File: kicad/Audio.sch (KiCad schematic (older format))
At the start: 14 parts, among them U4 OPA1664, U5 PGA4311, U6 OPA1664

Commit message: Adding untracked files
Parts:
- renumbered U4 to U3, U5 to U4, U6 to U5

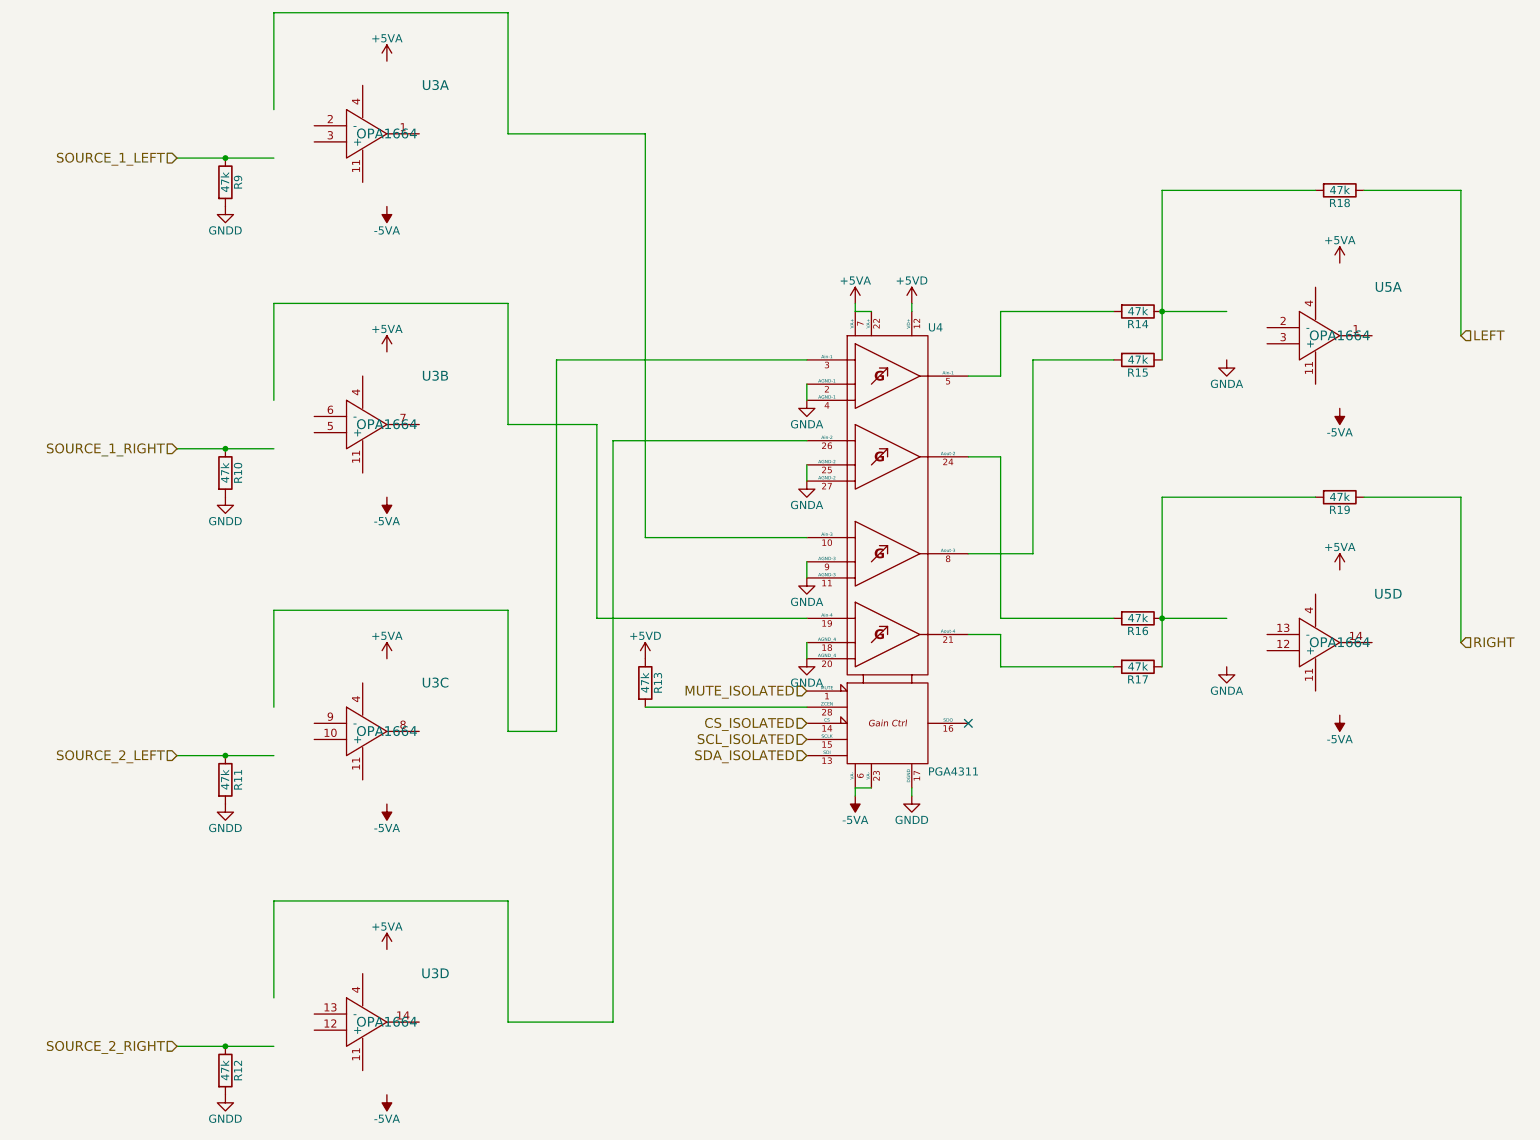
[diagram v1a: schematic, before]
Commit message: Reworked schematics to allow control of the power and introduction of ATMega328P for control
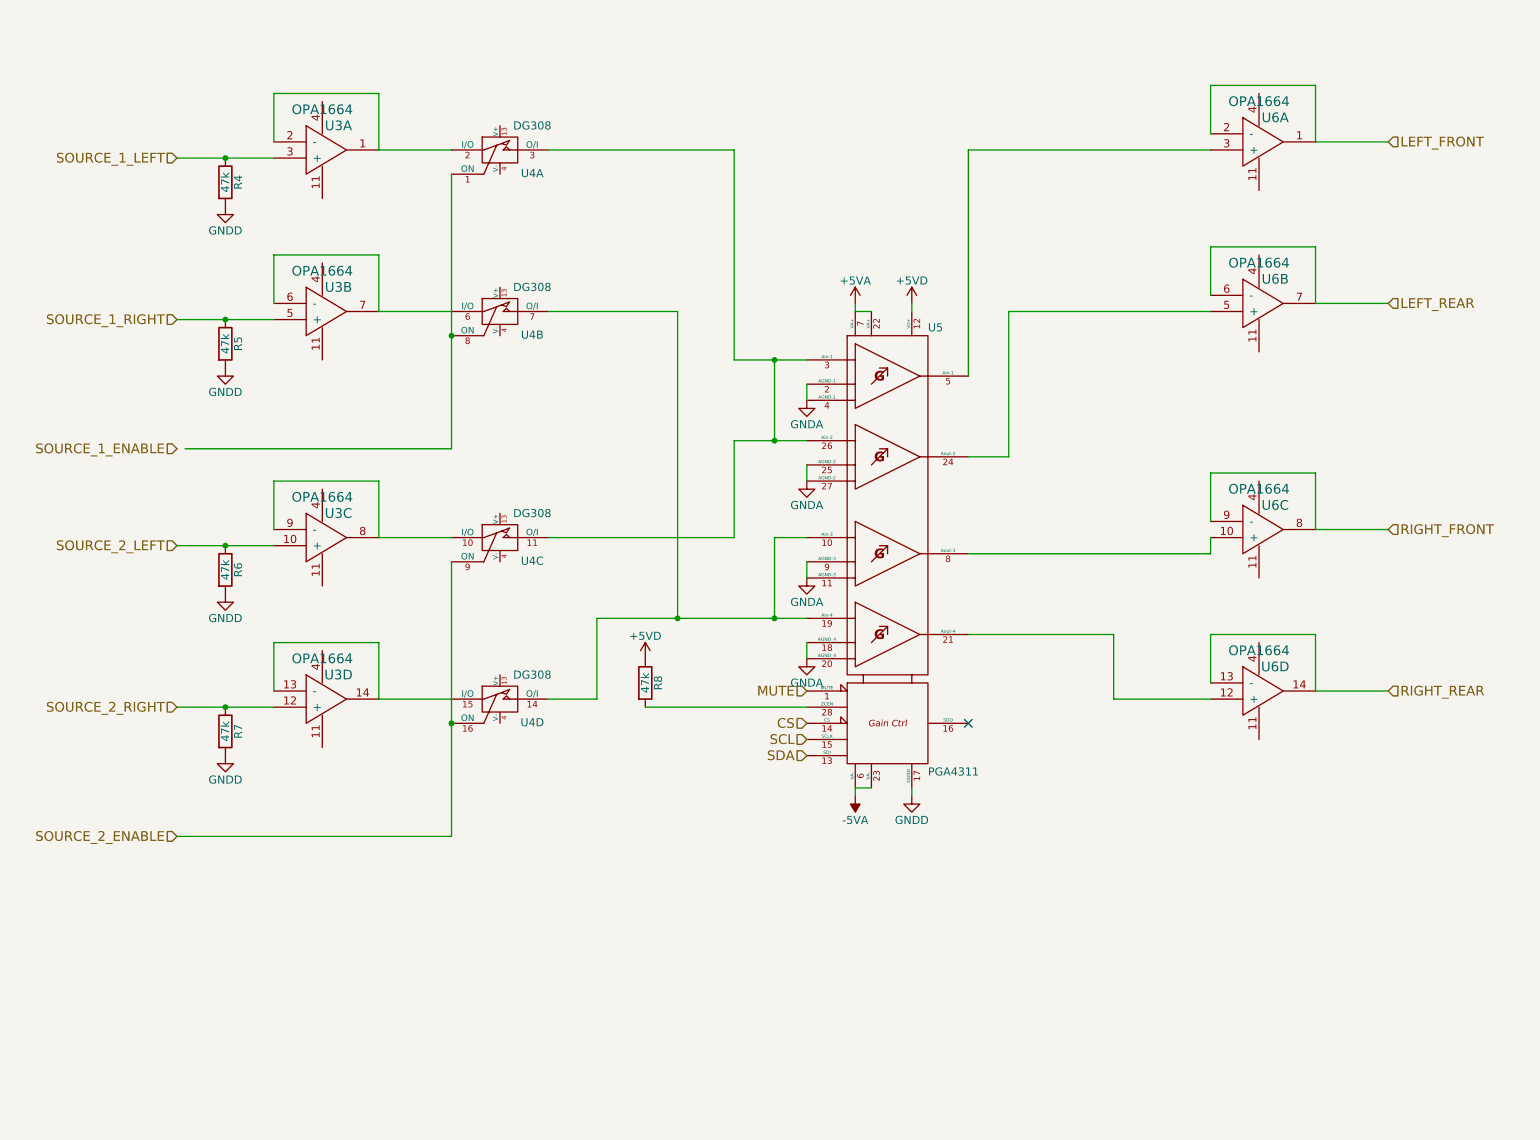
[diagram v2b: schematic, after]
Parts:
- removed R10, R11, R12, R14, R15, R16, R17, R18, R19: 47k, Resistors_SMD:R_0603_HandSoldering, symbol R
- removed U5: OPA1664, SMD_Packages:SOIC-14_N, symbol OPA1664
- added R5, R6, R7: 47k, Resistors_SMD:R_0603_HandSoldering, symbol R
- added U4: DG308, symbol DG308
- added U6: OPA1664, symbol OPA1664
- U3: footprint SMD_Packages:SOIC-14_N -> (none)
- renumbered R9 to R4, R13 to R8, U4 to U5
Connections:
- net labels added: CS, LEFT_FRONT, LEFT_REAR, MUTE, RIGHT_FRONT, RIGHT_REAR, SCL, SDA, SOURCE_1_ENABLE, SOURCE_2_ENABLE
- net labels removed: CS_ISOLATED, LEFT, MUTE_ISOLATED, RIGHT, SCL_ISOLATED, SDA_ISOLATED
- wire segments 61 -> 75

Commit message: Produced Volume knob including Gerbers, and updated main board to remove ERC errors.  Just about to start board layout
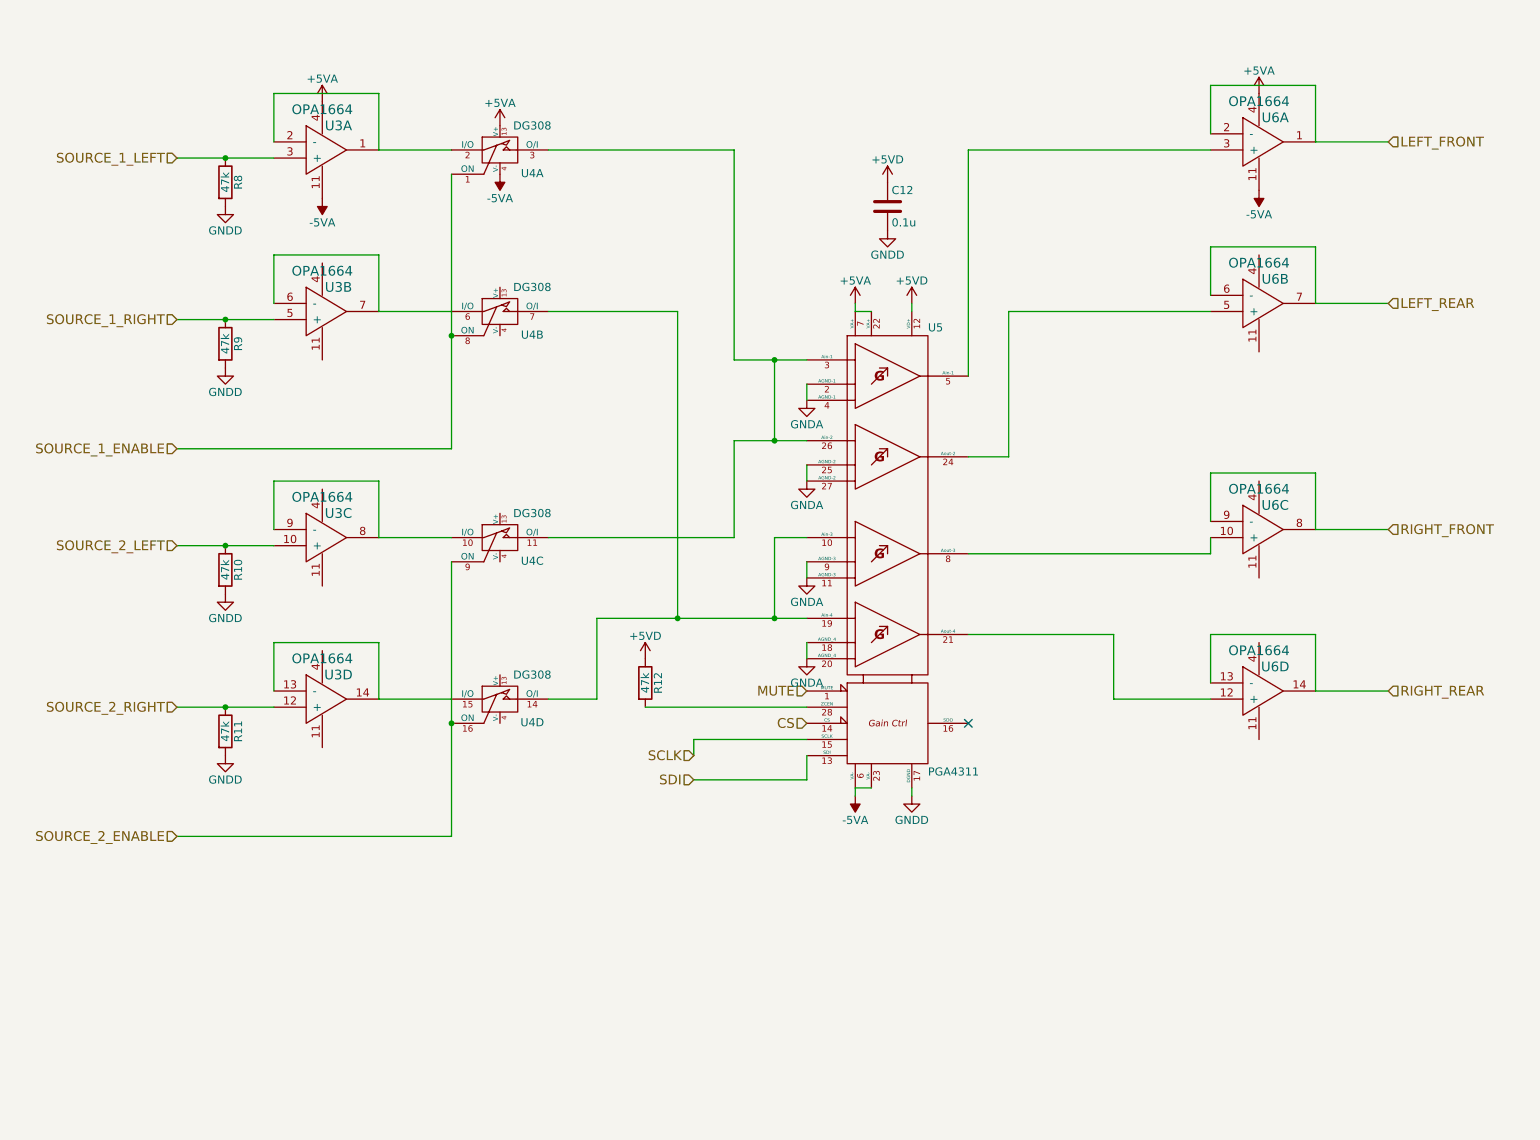
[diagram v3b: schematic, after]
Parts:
- added C12: 0.1u, Capacitors_SMD:C_0603_HandSoldering, symbol C
- U3, U6: footprint (none) -> SMD_Packages:SOIC-14_N
- U4: footprint (none) -> Housings_DIP:DIP-16_W7.62mm_LongPads
- renumbered R6 to R10, R7 to R11, R8 to R12, R4 to R8, R5 to R9
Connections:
- net +5VA: now also U3.4, U4.13 (V+), U6.4
- net +5VD: now also C12.1
- net -5VA: now also U3.11, U4.4 (V-), U6.11
- net GNDD: now also C12.2
- net SOURCE_1_ENABLE: now also U4.1 (ON), U4.8 (ON)
- net SCL renamed SCLK
- net SDA renamed SDI

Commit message: Routed the board.  Passes ERC check
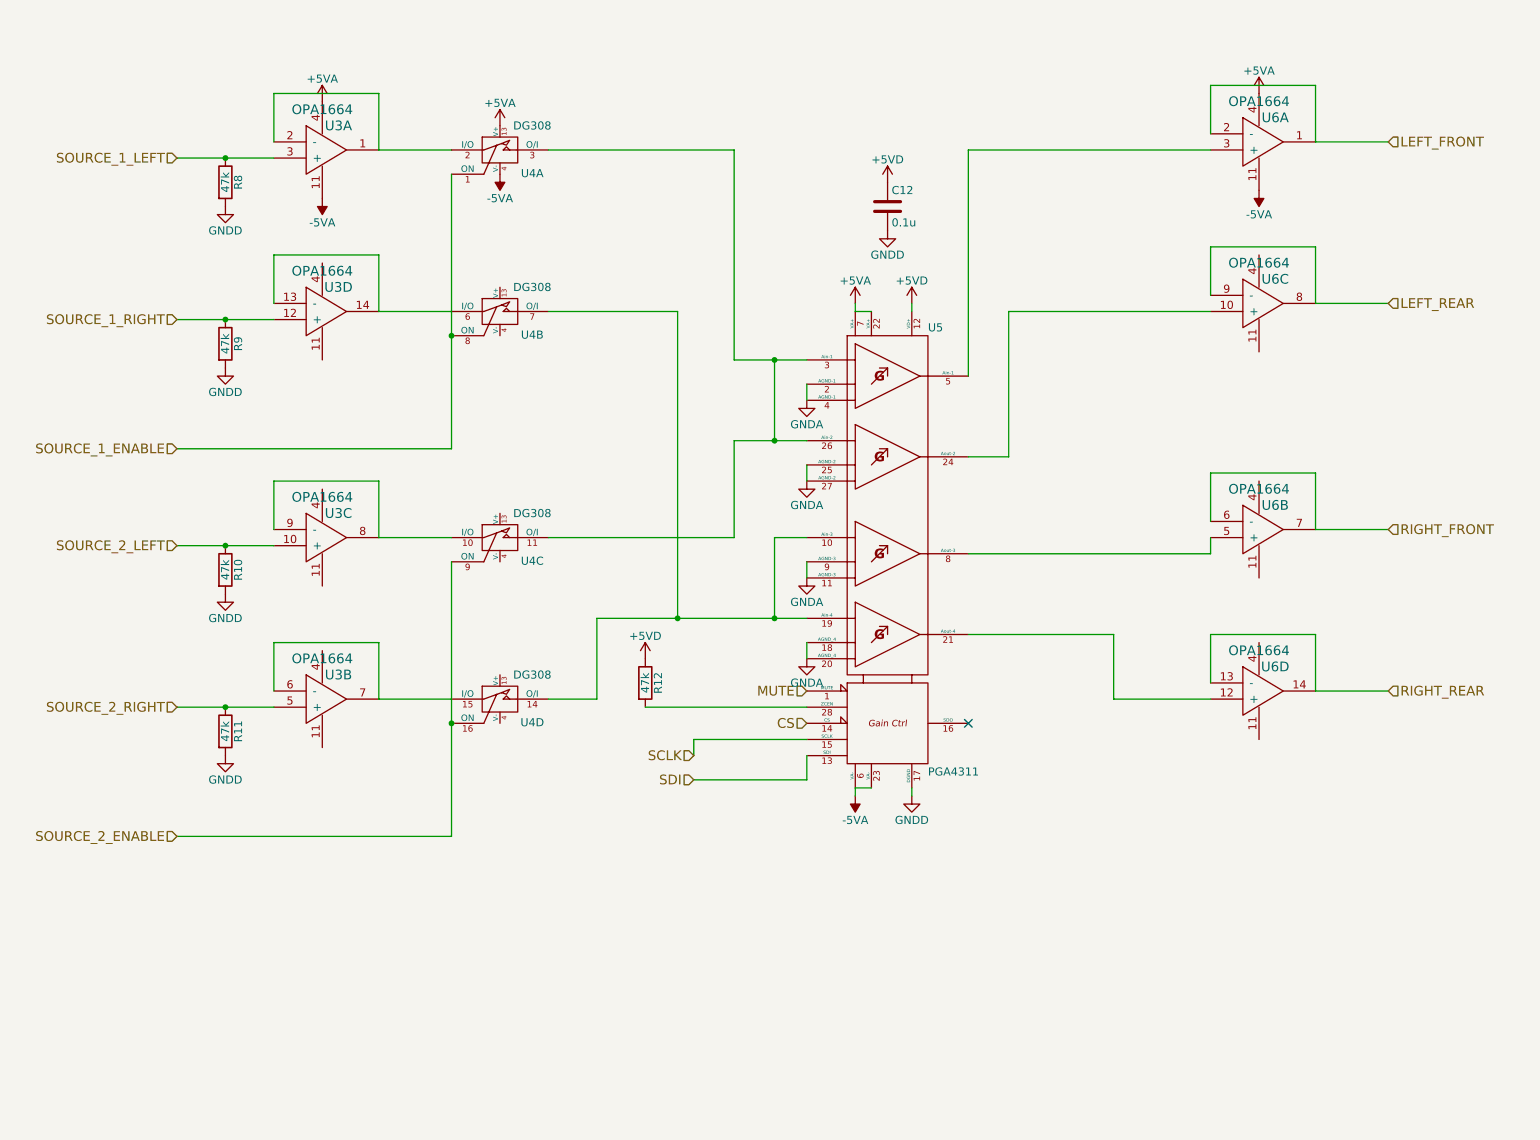
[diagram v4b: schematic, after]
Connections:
- net LEFT_REAR: now also U6.8, U6.9 (-); no longer U6.6 (-), U6.7
- net RIGHT_FRONT: now also U6.6 (-), U6.7; no longer U6.8, U6.9 (-)
- net SOURCE_1_RIGHT: now also U3.12 (+); no longer U3.5 (+)
- net SOURCE_2_RIGHT: now also U3.5 (+); no longer U3.12 (+)
- net at U5.24 (Aout-2): now also U6.10 (+); no longer U6.5 (+)
- net at U5.8 (Aout-3): now also U6.5 (+); no longer U6.10 (+)
- new net: U3.13 (-), U3.14, U4.6 (I/O)
- new net: U3.6 (-), U3.7, U4.15 (I/O)
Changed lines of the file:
@@
 $Comp
 L OPA1664 U3
-U 2 1 575EDD5C
+U 4 1 575EDD5C
 P 2550 2450
 F 0 "U3" H 2500 2600 60  0000 C CNN
@@
 F 2 "SMD_Packages:SOIC-14_N" H 2550 2450 60  0001 C CNN
 F 3 "" H 2550 2450 60  0000 C CNN
-	2    2550 2450
+	4    2550 2450
 	1    0    0    -1
 $EndComp
@@
 $Comp
 L OPA1664 U3
-U 4 1 575EDE92
+U 2 1 575EDE92
 P 2550 4850
 F 0 "U3" H 2500 5000 60  0000 C CNN
@@
 F 2 "SMD_Packages:SOIC-14_N" H 2550 4850 60  0001 C CNN
 F 3 "" H 2550 4850 60  0000 C CNN
-	4    2550 4850
+	2    2550 4850
 	1    0    0    -1
 $EndComp
@@
 $Comp
 L OPA1664 U6
-U 2 1 575EE92D
+U 3 1 575EE92D
 P 8350 2400
 F 0 "U6" H 8300 2550 60  0000 C CNN
@@
 F 2 "SMD_Packages:SOIC-14_N" H 8350 2400 60  0001 C CNN
 F 3 "" H 8350 2400 60  0000 C CNN
-	2    8350 2400
+	3    8350 2400
 	1    0    0    -1
 $EndComp
@@
 $Comp
 L OPA1664 U6
-U 3 1 575EE937
+U 2 1 575EE937
 P 8350 3800
 F 0 "U6" H 8300 3950 60  0000 C CNN
@@
 F 2 "SMD_Packages:SOIC-14_N" H 8350 3800 60  0001 C CNN
 F 3 "" H 8350 3800 60  0000 C CNN
-	3    8350 3800
-	1    0    0    -1
-$EndComp
+	2    8350 3800
+	1    0    0    -1
+$EndComp

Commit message: Updated board design with some footprint changes and improved audio layout
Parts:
- U4: footprint Housings_DIP:DIP-16_W7.62mm_LongPads -> Housings_SOIC:SOIC-16_3.9x9.9mm_Pitch1.27mm
- U5: footprint SMD_Packages:SOIC-28 -> Housings_SOIC:SOIC-28_7.5x17.9mm_Pitch1.27mm
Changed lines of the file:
@@
 F 0 "U5" H 6150 4750 50  0000 L CNN
 F 1 "PGA4311" H 6150 2000 50  0000 L CNN
-F 2 "SMD_Packages:SOIC-28" H 5900 3650 50  0001 C CNN
+F 2 "Housings_SOIC:SOIC-28_7.5x17.9mm_Pitch1.27mm" H 5900 3650 50  0001 C CNN
 F 3 "" H 5900 3650 50  0000 C CNN
 	1    5900 3650
@@
 F 0 "U4" H 3700 1305 50  0000 C CNN
 F 1 "DG308" H 3700 1600 50  0000 C CNN
-F 2 "Housings_DIP:DIP-16_W7.62mm_LongPads" H 3500 1450 60  0001 C CNN
+F 2 "Housings_SOIC:SOIC-16_3.9x9.9mm_Pitch1.27mm" H 3500 1450 60  0001 C CNN
 F 3 "" H 3500 1450 60  0000 C CNN
 	1    3500 1450
@@
 F 0 "U4" H 3700 2305 50  0000 C CNN
 F 1 "DG308" H 3700 2600 50  0000 C CNN
-F 2 "Housings_DIP:DIP-16_W7.62mm_LongPads" H 3500 2450 60  0001 C CNN
+F 2 "Housings_SOIC:SOIC-16_3.9x9.9mm_Pitch1.27mm" H 3500 2450 60  0001 C CNN
 F 3 "" H 3500 2450 60  0000 C CNN
 	2    3500 2450
@@
 F 0 "U4" H 3700 3705 50  0000 C CNN
 F 1 "DG308" H 3700 4000 50  0000 C CNN
-F 2 "Housings_DIP:DIP-16_W7.62mm_LongPads" H 3500 3850 60  0001 C CNN
+F 2 "Housings_SOIC:SOIC-16_3.9x9.9mm_Pitch1.27mm" H 3500 3850 60  0001 C CNN
 F 3 "" H 3500 3850 60  0000 C CNN
 	3    3500 3850
@@
 F 0 "U4" H 3700 4705 50  0000 C CNN
 F 1 "DG308" H 3700 5000 50  0000 C CNN
-F 2 "Housings_DIP:DIP-16_W7.62mm_LongPads" H 3500 4850 60  0001 C CNN
+F 2 "Housings_SOIC:SOIC-16_3.9x9.9mm_Pitch1.27mm" H 3500 4850 60  0001 C CNN
 F 3 "" H 3500 4850 60  0000 C CNN
 	4    3500 4850
